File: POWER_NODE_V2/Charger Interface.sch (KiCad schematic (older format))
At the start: 42 parts, among them J11 CONN_01X04, J12 CONN_01X04, J13 CONN_01X02, J14 CONN_01X02, J15 CONN_01X02, U15 TL783CKTTR, U16 TL783CKTTR, U17 AMC1100DWV, U18 AMC1100DWV, U19 NUD3124LT1G, U20 RTE24024

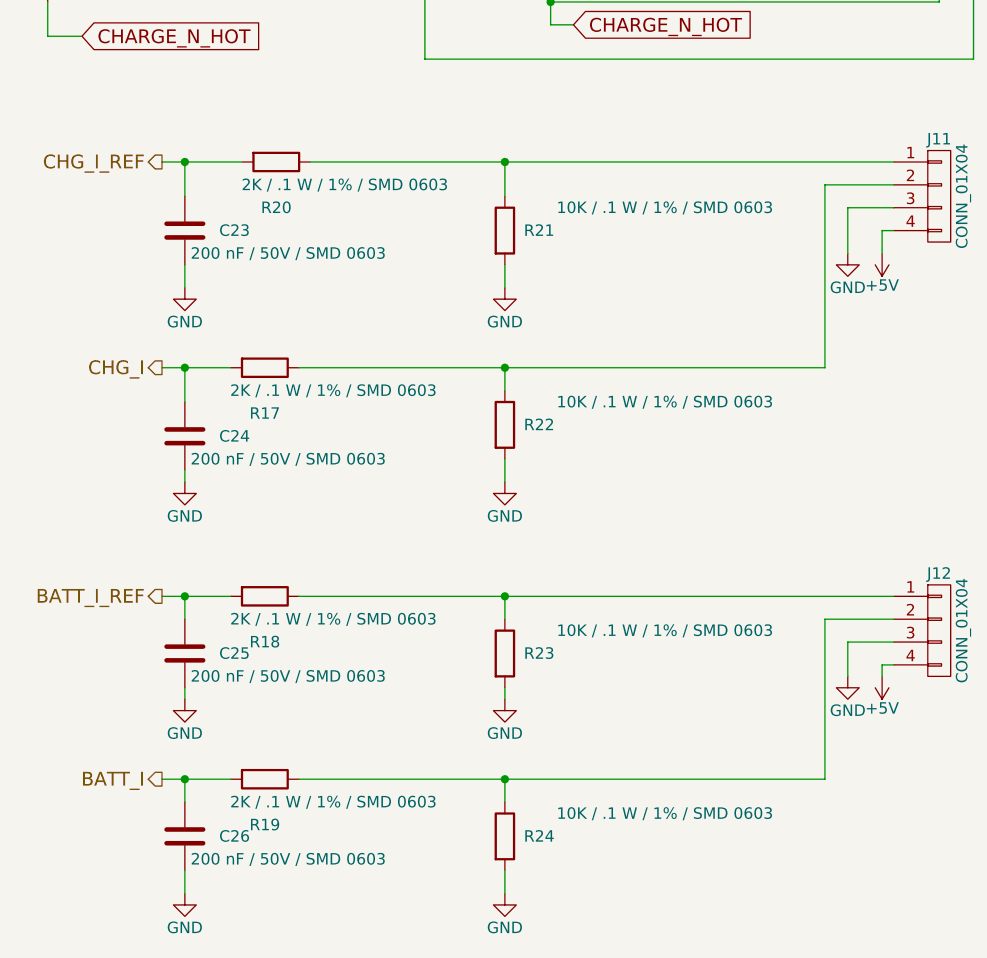
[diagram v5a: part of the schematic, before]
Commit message: Power Node v2 WIP
TODO: 3d models, double check everything, update connector P/N on
schematics, align boards and drill holes
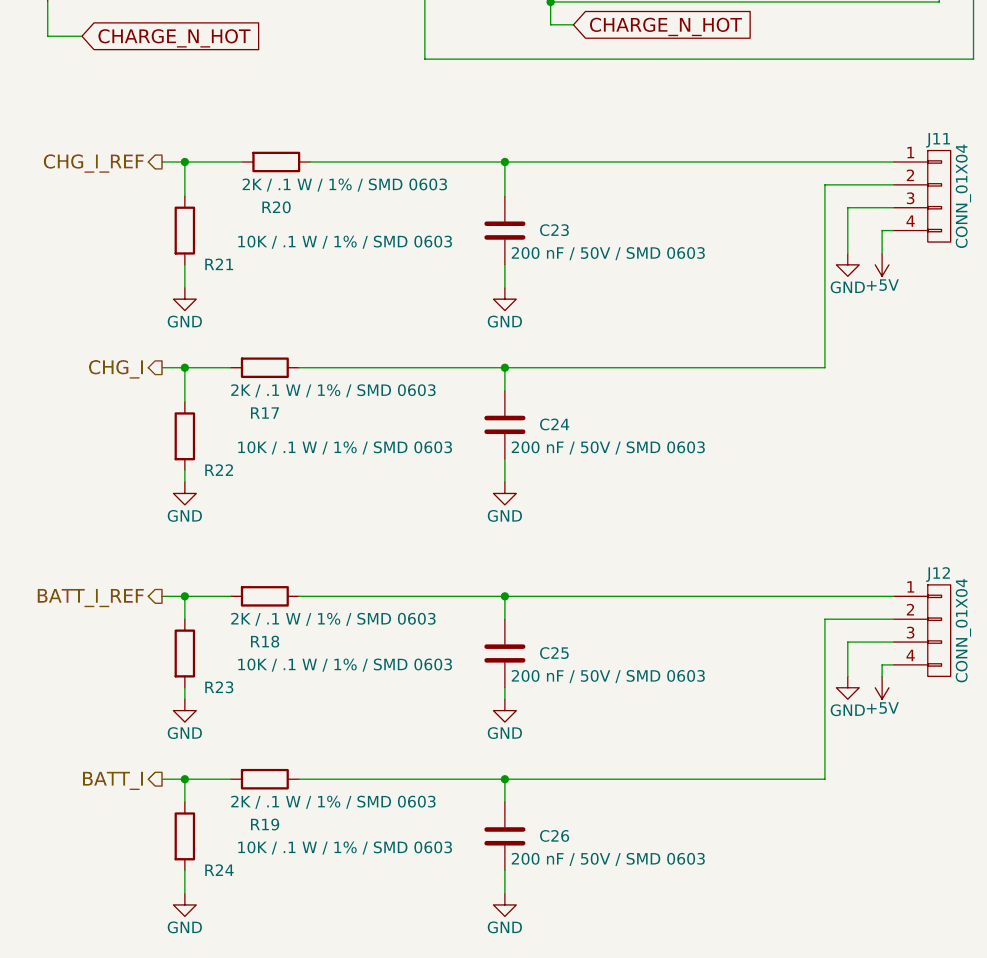
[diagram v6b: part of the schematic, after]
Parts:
- J11, J12: footprint Pin_Headers:Pin_Header_Straight_1x04_Pitch2.54mm -> rLoop Footprints:22-04-1041_Molex_4_Pin_Header_2.50mm
- J13, J14, J15: footprint Pin_Headers:Pin_Header_Straight_1x02_Pitch2.54mm -> rLoop Footprints:TE_1744055-2_3.96_EP_HDR_ASSY_2P_VERT_HT
- U15, U16: footprint TO_SOT_Packages_SMD:TO-263-3_TabPin2 -> TO_SOT_Packages_SMD:TO-263-3_TabPin4
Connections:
- net BATT_I: now also R24.1; no longer C26.1
- net BATT_I_REF: now also R23.1; no longer C25.1
- net CHG_I: now also R22.1; no longer C24.1
- net CHG_I_REF: now also R21.1; no longer C23.1
- net at J11.1 (P1), R20.1: now also C23.1; no longer R21.1
- net at J11.2 (P2), R17.1: now also C24.1; no longer R22.1
- net at J12.1 (P1), R18.1: now also C25.1; no longer R23.1
- net at J12.2 (P2), R19.1: now also C26.1; no longer R24.1
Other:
- moved on the sheet: C23, C24, C25, C26, R21, R22, R23, R24
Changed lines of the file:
@@
 F 0 "J11" H 4600 4850 50  0000 C CNN
 F 1 "CONN_01X04" V 4700 4600 50  0000 C CNN
-F 2 "Pin_Headers:Pin_Header_Straight_1x04_Pitch2.54mm" H 4600 4600 50  0001 C CNN
+F 2 "rLoop Footprints:22-04-1041_Molex_4_Pin_Header_2.50mm" H 4600 4600 50  0001 C CNN
 F 3 "" H 4600 4600 50  0001 C CNN
 	1    4600 4600
@@
 L R R21
 U 1 1 594DB63B
+P 1300 4750
+F 0 "R21" H 1450 4600 50  0000 C CNN
+F 1 "10K / .1 W / 1% / SMD 0603" H 2000 4700 50  0000 C CNN
+F 2 "Resistors_SMD:R_0603" V 1230 4750 50  0001 C CNN
+F 3 "" H 1300 4750 50  0001 C CNN
+	1    1300 4750
+	1    0    0    -1
+$EndComp
+$Comp
+L C C23
+U 1 1 594DB66C
 P 2700 4750
-F 0 "R21" H 2850 4750 50  0000 C CNN
-F 1 "10K / .1 W / 1% / SMD 0603" H 3400 4850 50  0000 C CNN
-F 2 "Resistors_SMD:R_0603" V 2630 4750 50  0001 C CNN
+F 0 "C23" H 2850 4750 50  0000 L CNN
+F 1 "200 nF / 50V / SMD 0603" H 2725 4650 50  0000 L CNN
+F 2 "Capacitors_SMD:C_0603" H 2738 4600 50  0001 C CNN
 F 3 "" H 2700 4750 50  0001 C CNN
 	1    2700 4750
-	1    0    0    -1
-$EndComp
-$Comp
-L C C23
-U 1 1 594DB66C
-P 1300 4750
-F 0 "C23" H 1450 4750 50  0000 L CNN
-F 1 "200 nF / 50V / SMD 0603" H 1325 4650 50  0000 L CNN
-F 2 "Capacitors_SMD:C_0603" H 1338 4600 50  0001 C CNN
-F 3 "" H 1300 4750 50  0001 C CNN
-	1    1300 4750
 	1    0    0    -1
 $EndComp
@@
 L R R22
 U 1 1 594DB8EC
+P 1300 5650
+F 0 "R22" H 1450 5500 50  0000 C CNN
+F 1 "10K / .1 W / 1% / SMD 0603" H 2000 5600 50  0000 C CNN
+F 2 "Resistors_SMD:R_0603" V 1230 5650 50  0001 C CNN
+F 3 "" H 1300 5650 50  0001 C CNN
+	1    1300 5650
+	1    0    0    -1
+$EndComp
+$Comp
+L C C24
+U 1 1 594DB917
 P 2700 5600
-F 0 "R22" H 2850 5600 50  0000 C CNN
-F 1 "10K / .1 W / 1% / SMD 0603" H 3400 5700 50  0000 C CNN
-F 2 "Resistors_SMD:R_0603" V 2630 5600 50  0001 C CNN
+F 0 "C24" H 2850 5600 50  0000 L CNN
+F 1 "200 nF / 50V / SMD 0603" H 2725 5500 50  0000 L CNN
+F 2 "Capacitors_SMD:C_0603" H 2738 5450 50  0001 C CNN
 F 3 "" H 2700 5600 50  0001 C CNN
 	1    2700 5600
-	1    0    0    -1
-$EndComp
-$Comp
-L C C24
-U 1 1 594DB917
-P 1300 5650
-F 0 "C24" H 1450 5650 50  0000 L CNN
-F 1 "200 nF / 50V / SMD 0603" H 1325 5550 50  0000 L CNN
-F 2 "Capacitors_SMD:C_0603" H 1338 5500 50  0001 C CNN
-F 3 "" H 1300 5650 50  0001 C CNN
-	1    1300 5650
 	1    0    0    -1
 $EndComp
@@
 F 0 "J12" H 4600 6750 50  0000 C CNN
 F 1 "CONN_01X04" V 4700 6500 50  0000 C CNN
-F 2 "Pin_Headers:Pin_Header_Straight_1x04_Pitch2.54mm" H 4600 6500 50  0001 C CNN
+F 2 "rLoop Footprints:22-04-1041_Molex_4_Pin_Header_2.50mm" H 4600 6500 50  0001 C CNN
 F 3 "" H 4600 6500 50  0001 C CNN
 	1    4600 6500
@@
 L R R23
 U 1 1 594DBD09
+P 1300 6600
+F 0 "R23" H 1450 6450 50  0000 C CNN
+F 1 "10K / .1 W / 1% / SMD 0603" H 2000 6550 50  0000 C CNN
+F 2 "Resistors_SMD:R_0603" V 1230 6600 50  0001 C CNN
+F 3 "" H 1300 6600 50  0001 C CNN
+	1    1300 6600
+	1    0    0    -1
+$EndComp
+$Comp
+L C C25
+U 1 1 594DBD0F
 P 2700 6600
-F 0 "R23" H 2850 6600 50  0000 C CNN
-F 1 "10K / .1 W / 1% / SMD 0603" H 3400 6700 50  0000 C CNN
-F 2 "Resistors_SMD:R_0603" V 2630 6600 50  0001 C CNN
+F 0 "C25" H 2850 6600 50  0000 L CNN
+F 1 "200 nF / 50V / SMD 0603" H 2725 6500 50  0000 L CNN
+F 2 "Capacitors_SMD:C_0603" H 2738 6450 50  0001 C CNN
 F 3 "" H 2700 6600 50  0001 C CNN
 	1    2700 6600
-	1    0    0    -1
-$EndComp
-$Comp
-L C C25
-U 1 1 594DBD0F
-P 1300 6600
-F 0 "C25" H 1450 6600 50  0000 L CNN
-F 1 "200 nF / 50V / SMD 0603" H 1325 6500 50  0000 L CNN
-F 2 "Capacitors_SMD:C_0603" H 1338 6450 50  0001 C CNN
-F 3 "" H 1300 6600 50  0001 C CNN
-	1    1300 6600
 	1    0    0    -1
 $EndComp
@@
 L R R24
 U 1 1 594DBD1B
+P 1300 7400
+F 0 "R24" H 1450 7250 50  0000 C CNN
+F 1 "10K / .1 W / 1% / SMD 0603" H 2000 7350 50  0000 C CNN
+F 2 "Resistors_SMD:R_0603" V 1230 7400 50  0001 C CNN
+F 3 "" H 1300 7400 50  0001 C CNN
+	1    1300 7400
+	1    0    0    -1
+$EndComp
+$Comp
+L C C26
+U 1 1 594DBD21
 P 2700 7400
-F 0 "R24" H 2850 7400 50  0000 C CNN
-F 1 "10K / .1 W / 1% / SMD 0603" H 3400 7500 50  0000 C CNN
-F 2 "Resistors_SMD:R_0603" V 2630 7400 50  0001 C CNN
+F 0 "C26" H 2850 7400 50  0000 L CNN
+F 1 "200 nF / 50V / SMD 0603" H 2725 7300 50  0000 L CNN
+F 2 "Capacitors_SMD:C_0603" H 2738 7250 50  0001 C CNN
 F 3 "" H 2700 7400 50  0001 C CNN
 	1    2700 7400
-	1    0    0    -1
-$EndComp
-$Comp
-L C C26
-U 1 1 594DBD21
-P 1300 7400
-F 0 "C26" H 1450 7400 50  0000 L CNN
-F 1 "200 nF / 50V / SMD 0603" H 1325 7300 50  0000 L CNN
-F 2 "Capacitors_SMD:C_0603" H 1338 7250 50  0001 C CNN
-F 3 "" H 1300 7400 50  0001 C CNN
-	1    1300 7400
 	1    0    0    -1
 $EndComp
@@
 F 0 "J15" H 10100 5700 50  0000 C CNN
 F 1 "CONN_01X02" V 10200 5550 50  0000 C CNN
-F 2 "Pin_Headers:Pin_Header_Straight_1x02_Pitch2.54mm" H 10100 5550 50  0001 C CNN
+F 2 "rLoop Footprints:TE_1744055-2_3.96_EP_HDR_ASSY_2P_VERT_HT" H 10100 5550 50  0001 C CNN
 F 3 "" H 10100 5550 50  0001 C CNN
 	1    10100 5550
@@
 F 0 "U15" H 2050 1400 60  0000 C CNN
 F 1 "TL783CKTTR" H 2250 1500 60  0000 C CNN
-F 2 "TO_SOT_Packages_SMD:TO-263-3_TabPin2" H 2300 1150 60  0001 C CNN
+F 2 "TO_SOT_Packages_SMD:TO-263-3_TabPin4" H 2300 1150 60  0001 C CNN
 F 3 "" H 2300 1150 60  0001 C CNN
 	1    2300 1150
@@
 F 0 "U16" H 2050 3050 60  0000 C CNN
 F 1 "TL783CKTTR" H 2250 3150 60  0000 C CNN
-F 2 "TO_SOT_Packages_SMD:TO-263-3_TabPin2" H 2300 2800 60  0001 C CNN
+F 2 "TO_SOT_Packages_SMD:TO-263-3_TabPin4" H 2300 2800 60  0001 C CNN
 F 3 "" H 2300 2800 60  0001 C CNN
 	1    2300 2800
@@
 F 0 "J14" H 9600 1600 50  0000 C CNN
 F 1 "CONN_01X02" V 9700 1450 50  0000 C CNN
-F 2 "Pin_Headers:Pin_Header_Straight_1x02_Pitch2.54mm" H 9600 1450 50  0001 C CNN
+F 2 "rLoop Footprints:TE_1744055-2_3.96_EP_HDR_ASSY_2P_VERT_HT" H 9600 1450 50  0001 C CNN
 F 3 "" H 9600 1450 50  0001 C CNN
 	1    9600 1450
@@
 F 0 "J13" H 9550 2200 50  0000 C CNN
 F 1 "CONN_01X02" V 9650 2050 50  0000 C CNN
-F 2 "Pin_Headers:Pin_Header_Straight_1x02_Pitch2.54mm" H 9550 2050 50  0001 C CNN
+F 2 "rLoop Footprints:TE_1744055-2_3.96_EP_HDR_ASSY_2P_VERT_HT" H 9550 2050 50  0001 C CNN
 F 3 "" H 9550 2050 50  0001 C CNN
 	1    9550 2050
@@
 Charger & Batt I/O
 Wire Wire Line
-	1200 5350 1500 5350
-Wire Wire Line
-	1300 5350 1300 5500
-Connection ~ 1300 5350
-Wire Wire Line
-	1800 5350 4100 5350
-Wire Wire Line
-	2700 5350 2700 5450
-Wire Wire Line
-	1200 4450 1550 4450
-Wire Wire Line
-	1300 4450 1300 4600
-Connection ~ 1300 4450
-Wire Wire Line
-	1850 4450 4400 4450
-Wire Wire Line
-	2700 4600 2700 4450
-Connection ~ 2700 4450
-Wire Wire Line
 	4100 4550 4400 4550
 Wire Wire Line
 	4100 5350 4100 4550
-Connection ~ 2700 5350
 Wire Wire Line
 	4350 4850 4350 4750
@@
 	4200 4650 4400 4650
 Wire Wire Line
-	1200 7150 1500 7150
-Wire Wire Line
-	1300 7150 1300 7250
-Connection ~ 1300 7150
-Wire Wire Line
-	1800 7150 4100 7150
-Wire Wire Line
-	2700 7150 2700 7250
-Wire Wire Line
-	1200 6350 1500 6350
-Wire Wire Line
-	1300 6350 1300 6450
-Connection ~ 1300 6350
-Wire Wire Line
-	1800 6350 4400 6350
-Wire Wire Line
-	2700 6350 2700 6450
-Connection ~ 2700 6350
-Wire Wire Line
 	4100 7150 4100 6450
-Connection ~ 2700 7150
 Wire Wire Line
 	2700 6800 2700 6750
@@
 	0    -1   -1   0
 $EndComp
+Wire Wire Line
+	1200 4450 1550 4450
+Wire Wire Line
+	1850 4450 4400 4450
+Wire Wire Line
+	4100 5350 1800 5350
+Wire Wire Line
+	1500 5350 1200 5350
+Wire Wire Line
+	1300 5500 1300 5350
+Connection ~ 1300 5350
+Wire Wire Line
+	2700 5450 2700 5350
+Connection ~ 2700 5350
+Wire Wire Line
+	1300 4600 1300 4450
+Connection ~ 1300 4450
+Wire Wire Line
+	2700 4600 2700 4450
+Connection ~ 2700 4450
+Wire Wire Line
+	1200 6350 1500 6350
+Wire Wire Line
+	1300 6350 1300 6450
+Connection ~ 1300 6350
+Wire Wire Line
+	1800 6350 4400 6350
+Wire Wire Line
+	2700 6450 2700 6350
+Connection ~ 2700 6350
+Wire Wire Line
+	1200 7150 1500 7150
+Wire Wire Line
+	1300 7150 1300 7250
+Connection ~ 1300 7150
+Wire Wire Line
+	1800 7150 4100 7150
+Wire Wire Line
+	2700 7250 2700 7150
+Connection ~ 2700 7150
 $EndSCHEMATC

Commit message: Lot's of progress
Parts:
- D8: footprint rLoop Footprints:LED_0805 -> rLoop_Footprints:LED_0805
- J11, J12: footprint rLoop Footprints:22-04-1041_Molex_4_Pin_Header_2.50mm -> rLoop_Footprints:22-04-1041_Molex_4_Pin_Header_2.50mm
- J13, J14, J15: value CONN_01X02 -> TE_3-641119-2; footprint rLoop Footprints:TE_1744055-2_3.96_EP_HDR_ASSY_2P_VERT_HT -> rLoop_Footprints:3-641119-2_TE_2P_MTA156_HDR
- U17, U18: footprint rLoop Footprints:amc1100_SOIC8 -> rLoop_Footprints:amc1100_SOIC8
- U20: footprint rLoop Footprints:RTE24024 -> rLoop_Footprints:RTE24024
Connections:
- net BATT_N_HOT: now also J14.1 (P1); no longer J14.2 (P2)
- net BATT_P_HOT: now also J14.2 (P2); no longer J14.1 (P1)
- net CHARGE_N_HOT: now also J13.1 (P1); no longer J13.2 (P2)
- net CHARGE_P_HOT: now also J13.2 (P2); no longer J13.1 (P1)
- net GND: now also J15.1 (P1); no longer J15.2 (P2)
- net at D8.2 (A), D9.1 (K), U20.14: now also J15.2 (P2); no longer J15.1 (P1)
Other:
- moved on the sheet: D9, J13, J14, J15
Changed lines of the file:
@@
 F 0 "J11" H 4600 4850 50  0000 C CNN
 F 1 "CONN_01X04" V 4700 4600 50  0000 C CNN
-F 2 "rLoop Footprints:22-04-1041_Molex_4_Pin_Header_2.50mm" H 4600 4600 50  0001 C CNN
+F 2 "rLoop_Footprints:22-04-1041_Molex_4_Pin_Header_2.50mm" H 4600 4600 50  0001 C CNN
 F 3 "" H 4600 4600 50  0001 C CNN
 	1    4600 4600
@@
 F 0 "J12" H 4600 6750 50  0000 C CNN
 F 1 "CONN_01X04" V 4700 6500 50  0000 C CNN
-F 2 "rLoop Footprints:22-04-1041_Molex_4_Pin_Header_2.50mm" H 4600 6500 50  0001 C CNN
+F 2 "rLoop_Footprints:22-04-1041_Molex_4_Pin_Header_2.50mm" H 4600 6500 50  0001 C CNN
 F 3 "" H 4600 6500 50  0001 C CNN
 	1    4600 6500
@@
 F 0 "U20" H 8220 5300 60  0000 C CNN
 F 1 "RTE24024" H 8390 5190 60  0000 C CNN
-F 2 "rLoop Footprints:RTE24024" H 7650 5250 60  0001 C CNN
+F 2 "rLoop_Footprints:RTE24024" H 7650 5250 60  0001 C CNN
 F 3 "" H 7650 5250 60  0001 C CNN
 	1    7650 5250
@@
 L CONN_01X02 J15
 U 1 1 59500087
-P 10100 5550
-F 0 "J15" H 10100 5700 50  0000 C CNN
-F 1 "CONN_01X02" V 10200 5550 50  0000 C CNN
-F 2 "rLoop Footprints:TE_1744055-2_3.96_EP_HDR_ASSY_2P_VERT_HT" H 10100 5550 50  0001 C CNN
-F 3 "" H 10100 5550 50  0001 C CNN
-	1    10100 5550
-	0    1    1    0
-$EndComp
-Text Notes 9700 5900 0    60   ~ 0
+P 9850 5100
+F 0 "J15" H 9850 5250 50  0000 C CNN
+F 1 "TE_3-641119-2" V 9950 5100 50  0000 C CNN
+F 2 "rLoop_Footprints:3-641119-2_TE_2P_MTA156_HDR" H 9850 5100 50  0001 C CNN
+F 3 "" H 9850 5100 50  0001 C CNN
+	1    9850 5100
+	-1   0    0    1
+$EndComp
+Text Notes 9750 5650 0    60   ~ 0
 Charger Relay\nMax 8A
 $Comp
 L D D9
 U 1 1 595001A3
-P 9200 4850
-F 0 "D9" V 9250 5000 50  0000 C CNN
-F 1 "1N4004" V 9150 5100 50  0000 C CNN
-F 2 "Diodes_THT:D_DO-201_P15.24mm_Horizontal" H 9200 4850 50  0001 C CNN
-F 3 "" H 9200 4850 50  0001 C CNN
-	1    9200 4850
+P 9200 5000
+F 0 "D9" V 9250 5150 50  0000 C CNN
+F 1 "1N4004" V 9150 5250 50  0000 C CNN
+F 2 "Diodes_THT:D_DO-201_P15.24mm_Horizontal" H 9200 5000 50  0001 C CNN
+F 3 "" H 9200 5000 50  0001 C CNN
+	1    9200 5000
 	0    1    1    0
 $EndComp
@@
 L GND #PWR0125
 U 1 1 595004C9
-P 9200 5100
-F 0 "#PWR0125" H 9200 4850 50  0001 C CNN
-F 1 "GND" H 9200 4950 50  0000 C CNN
-F 2 "" H 9200 5100 50  0001 C CNN
-F 3 "" H 9200 5100 50  0001 C CNN
-	1    9200 5100
+P 9200 5600
+F 0 "#PWR0125" H 9200 5350 50  0001 C CNN
+F 1 "GND" H 9200 5450 50  0000 C CNN
+F 2 "" H 9200 5600 50  0001 C CNN
+F 3 "" H 9200 5600 50  0001 C CNN
+	1    9200 5600
 	1    0    0    -1
 $EndComp
@@
 F 0 "U18" H 5200 3050 60  0000 C CNN
 F 1 "AMC1100DWV" H 5450 3150 60  0000 C CNN
-F 2 "rLoop Footprints:amc1100_SOIC8" H 5400 2800 60  0001 C CNN
+F 2 "rLoop_Footprints:amc1100_SOIC8" H 5400 2800 60  0001 C CNN
 F 3 "" H 5400 2800 60  0001 C CNN
 	1    5400 2800
@@
 	1    0    0    -1
 $EndComp
-Text GLabel 9050 1400 0    60   Input ~ 0
+Text GLabel 9050 1700 0    60   Input ~ 0
 BATT_P_HOT
 Text GLabel 9050 1550 0    60   Input ~ 0
@@
 Text GLabel 9050 2150 0    60   Input ~ 0
 CHARGE_N_HOT
-Text GLabel 9050 2000 0    60   Input ~ 0
+Text GLabel 9050 2300 0    60   Input ~ 0
 CHARGE_P_HOT
 Text GLabel 3000 2100 2    60   Input ~ 0
@@
 F 0 "U17" H 5200 1400 60  0000 C CNN
 F 1 "AMC1100DWV" H 5450 1500 60  0000 C CNN
-F 2 "rLoop Footprints:amc1100_SOIC8" H 5400 1150 60  0001 C CNN
+F 2 "rLoop_Footprints:amc1100_SOIC8" H 5400 1150 60  0001 C CNN
 F 3 "" H 5400 1150 60  0001 C CNN
 	1    5400 1150
@@
 L CONN_01X02 J14
 U 1 1 59516F89
-P 9600 1450
-F 0 "J14" H 9600 1600 50  0000 C CNN
-F 1 "CONN_01X02" V 9700 1450 50  0000 C CNN
-F 2 "rLoop Footprints:TE_1744055-2_3.96_EP_HDR_ASSY_2P_VERT_HT" H 9600 1450 50  0001 C CNN
-F 3 "" H 9600 1450 50  0001 C CNN
-	1    9600 1450
+P 9600 1600
+F 0 "J14" H 9600 1750 50  0000 C CNN
+F 1 "TE_3-641119-2" V 9700 1600 50  0000 C CNN
+F 2 "rLoop_Footprints:3-641119-2_TE_2P_MTA156_HDR" H 9600 1600 50  0001 C CNN
+F 3 "" H 9600 1600 50  0001 C CNN
+	1    9600 1600
 	1    0    0    -1
 $EndComp
@@
 L CONN_01X02 J13
 U 1 1 59517025
-P 9550 2050
-F 0 "J13" H 9550 2200 50  0000 C CNN
-F 1 "CONN_01X02" V 9650 2050 50  0000 C CNN
-F 2 "rLoop Footprints:TE_1744055-2_3.96_EP_HDR_ASSY_2P_VERT_HT" H 9550 2050 50  0001 C CNN
-F 3 "" H 9550 2050 50  0001 C CNN
-	1    9550 2050
+P 9550 2200
+F 0 "J13" H 9550 2350 50  0000 C CNN
+F 1 "TE_3-641119-2" V 9650 2200 50  0000 C CNN
+F 2 "rLoop_Footprints:3-641119-2_TE_2P_MTA156_HDR" H 9550 2200 50  0001 C CNN
+F 3 "" H 9550 2200 50  0001 C CNN
+	1    9550 2200
 	1    0    0    -1
 $EndComp
@@
 	8050 4700 10150 4700
 Wire Wire Line
-	9200 5000 10050 5000
+	9200 5450 10150 5450
 Wire Wire Line
 	8050 4850 8050 4700
 Connection ~ 9200 4700
 Wire Wire Line
-	9200 5100 9200 5000
+	9200 5150 9200 5600
 Wire Wire Line
 	8950 5750 8950 5050
@@
 Connection ~ 2900 2000
 Wire Wire Line
-	10150 4700 10150 5350
-Wire Wire Line
-	10050 5000 10050 5350
-Wire Wire Line
 	4900 1850 5150 1850
 Wire Wire Line
@@
 Wire Wire Line
 	7050 900  6750 900
-Wire Wire Line
-	9050 1400 9400 1400
-Wire Wire Line
-	9400 1500 9200 1500
-Wire Wire Line
-	9200 1500 9200 1550
-Wire Wire Line
-	9200 1550 9050 1550
-Wire Wire Line
-	9050 2000 9350 2000
-Wire Wire Line
-	9350 2100 9200 2100
-Wire Wire Line
-	9200 2100 9200 2150
-Wire Wire Line
-	9200 2150 9050 2150
 Wire Wire Line
 	5950 3250 5950 3600
@@
 F 0 "D8" V 8850 5150 50  0000 C CNN
 F 1 "EL-17-21VGC/TR8" V 8950 5350 50  0000 C CNN
-F 2 "rLoop Footprints:LED_0805" H 8950 4900 50  0001 C CNN
+F 2 "rLoop_Footprints:LED_0805" H 8950 4900 50  0001 C CNN
 F 3 "" H 8950 4900 50  0001 C CNN
 	1    8950 4900
@@
 	1850 4450 4400 4450
 Wire Wire Line
-	4100 5350 1800 5350
-Wire Wire Line
-	1500 5350 1200 5350
+	1800 5350 4100 5350
+Wire Wire Line
+	1200 5350 1500 5350
 Wire Wire Line
 	1300 5500 1300 5350
@@
 	2700 7250 2700 7150
 Connection ~ 2700 7150
+Wire Wire Line
+	9050 2150 9350 2150
+Wire Wire Line
+	9350 2250 9050 2250
+Wire Wire Line
+	9050 2250 9050 2300
+Wire Wire Line
+	9400 1550 9050 1550
+Wire Wire Line
+	9050 1700 9400 1700
+Wire Wire Line
+	9400 1700 9400 1650
+Wire Wire Line
+	9200 4850 9200 4700
+Connection ~ 9200 5450
+Wire Wire Line
+	10150 4700 10150 5050
+Wire Wire Line
+	10150 5050 10050 5050
+Wire Wire Line
+	10050 5150 10150 5150
+Wire Wire Line
+	10150 5150 10150 5450
 $EndSCHEMATC
